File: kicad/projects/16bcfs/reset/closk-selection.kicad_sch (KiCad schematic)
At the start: 3 parts, among them U2 74HC00, U3 74HC08, U4 74HC32

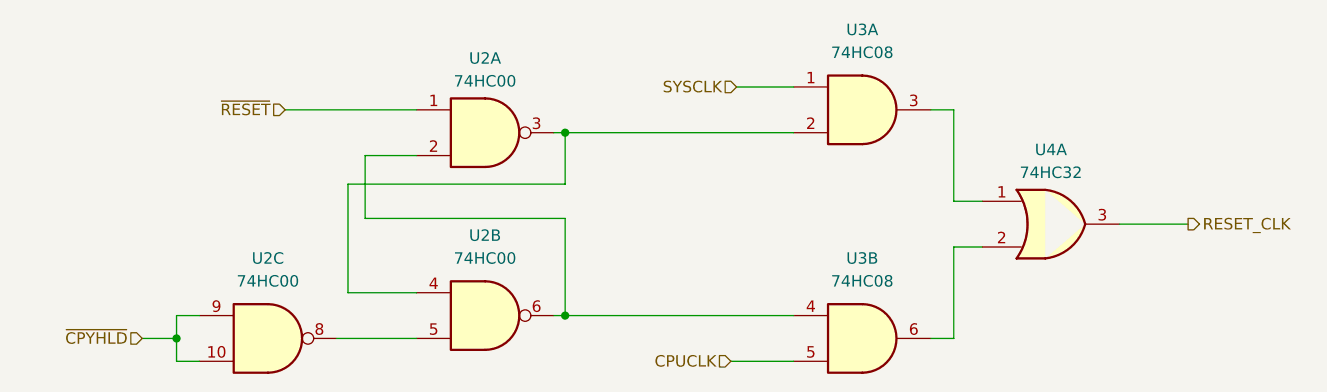
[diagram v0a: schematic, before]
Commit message: Added some debugging code
This is still not working.  I will need to revamp the reset routines for
the emulator to get this to work properly.  Everything will need an
initial state on construction and a `reset()` routine to place
everything into a proper state.  This in itself will be a major change.
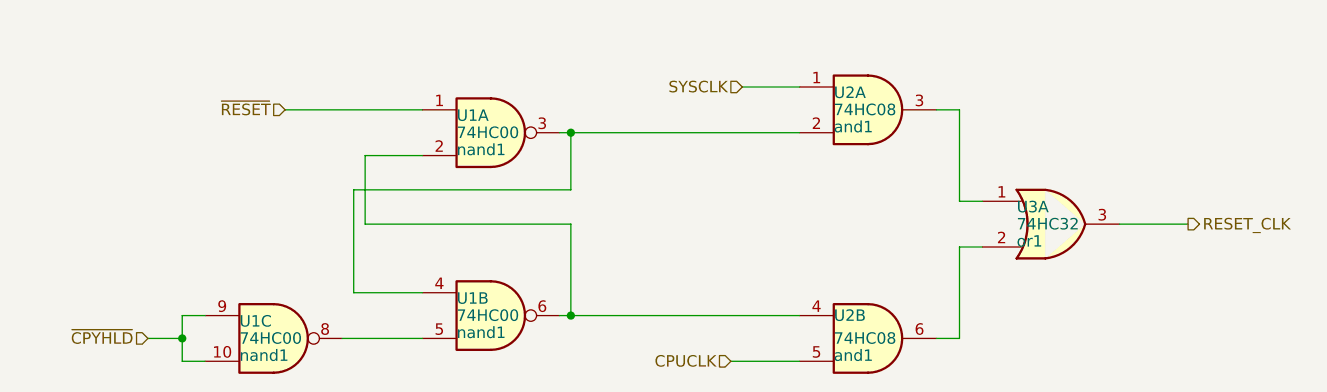
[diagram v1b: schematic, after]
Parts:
- U1: renamed from U2; name (none) -> nand1
- U2: renamed from U3; name (none) -> and1
- U3: renamed from U4; name (none) -> or1
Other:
- moved on the sheet: U1A, U1B, U1C, U2A, U2B

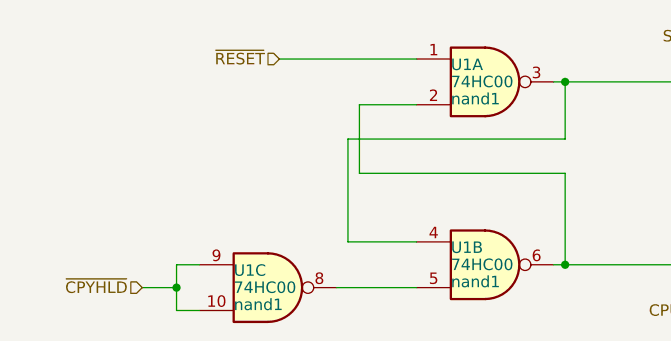
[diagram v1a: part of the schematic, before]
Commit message: Make a number of changes to the schematic and emulator
These changes are incremental to getting the emulator to work, they are
needed for making sure that the RESETTING, CLOCKING, and RUNNING signals
are processed properly.

There is also quite a bit of debugging code which gets added/removed
ahead of this commit.
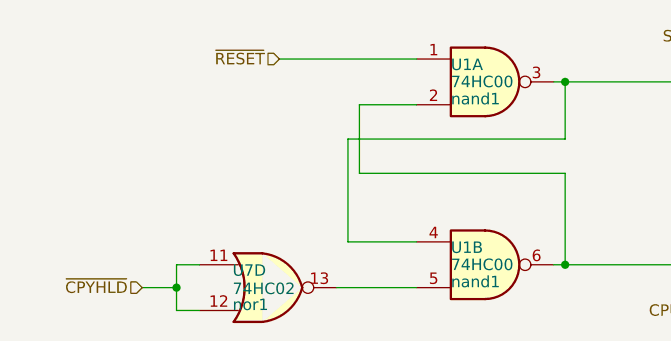
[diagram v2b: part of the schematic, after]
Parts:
- removed unit 3 of U1
- added U7: 74HC02, symbol 74xx:74HC02
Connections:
- net ~{CPYHLD}: now also U7.11, U7.12
- net at U1.5: now also U7.13

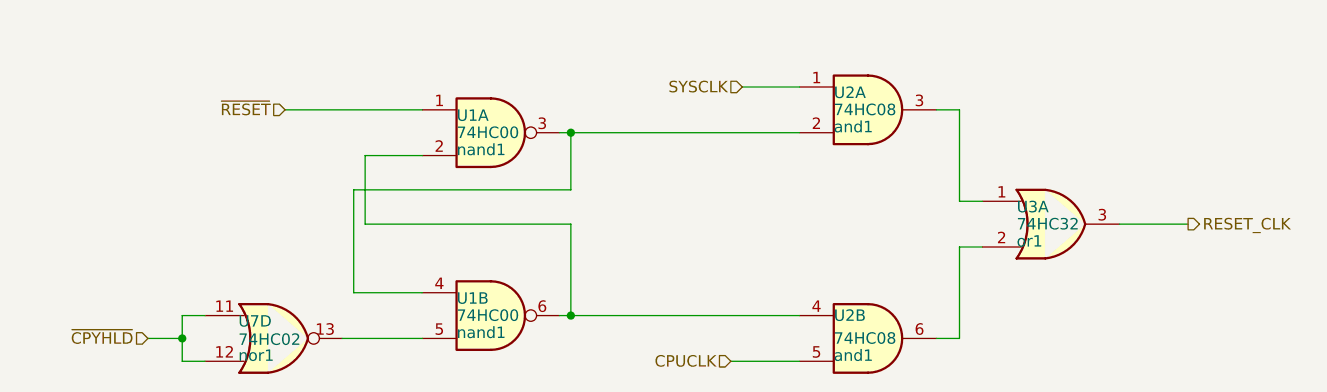
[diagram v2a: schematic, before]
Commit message: Relocate the unused gates for efficiency
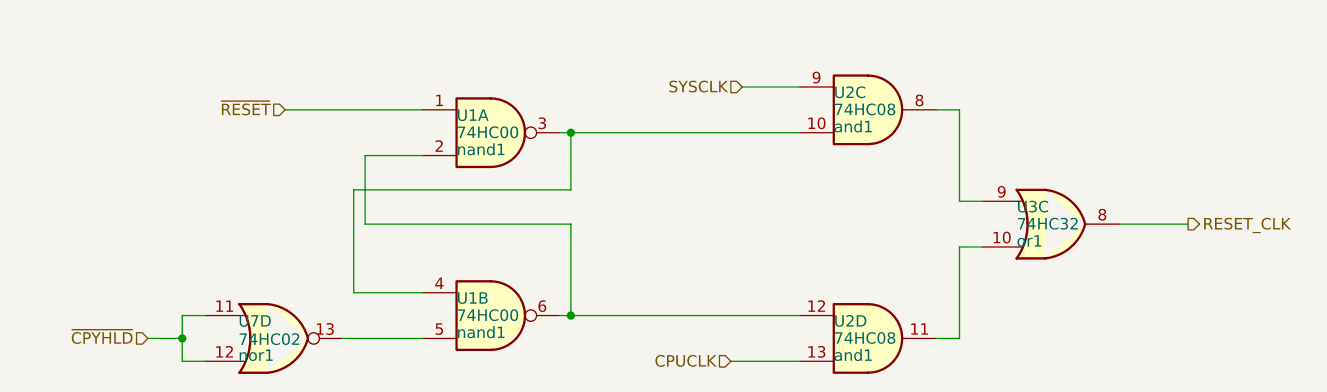
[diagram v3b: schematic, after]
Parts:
- removed U2: 74HC08, symbol eryjus:74HC08
- removed U3: 74HC32, symbol eryjus:74HC32
- added U2: 74HC08, symbol eryjus:74HC08
- added U3: 74HC32, symbol eryjus:74HC32
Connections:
- net CPUCLK: now also U2.13
- net RESET_CLK: now also U3.8
- net SYSCLK: now also U2.9
- net at U1.3, U1.4: now also U2.10
- net at U1.2, U1.6: now also U2.12
- new net: U2.8, U3.9
- new net: U2.11, U3.10
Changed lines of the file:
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@@
   (netclass_flag "" (length 2.54) (shape round) (at 190.5 90.17 180)
     (effects (font (size 1.27 1.27)) (justify right bottom))
-    (property "Netclass" "or1-Y1" (at 191.1985 92.71 0)
+    (property "Netclass" "or1-Y3" (at 191.1985 92.71 0)
       (effects (font (size 1.27 1.27) italic) (justify left))
     )
@@
   (netclass_flag "" (length 2.54) (shape round) (at 170.18 102.87 180)
     (effects (font (size 1.27 1.27)) (justify right bottom))
-    (property "Netclass" "and1-Y2" (at 170.8785 105.41 0)
+    (property "Netclass" "and1-Y3" (at 170.8785 105.41 0)
       (effects (font (size 1.27 1.27) italic) (justify left))
     )
@@
   (netclass_flag "" (length 2.54) (shape round) (at 170.18 77.47 0)
     (effects (font (size 1.27 1.27)) (justify left bottom))
-    (property "Netclass" "and1-Y1" (at 170.8785 74.93 0)
-      (effects (font (size 1.27 1.27) italic) (justify left))
+    (property "Netclass" "and1-Y3" (at 170.8785 74.93 0)
+      (effects (font (size 1.27 1.27) italic) (justify left))
+    )
+  )
+  (symbol (lib_id "eryjus:74HC08") (at 162.56 77.47 0) (unit 3)
+    (in_bom yes) (on_board yes) (dnp no)
+    (property "Reference" "U2" (at 158.75 75.565 0)
+      (effects (font (size 1.27 1.27)) (justify left))
+    )
+    (property "Value" "74HC08" (at 158.75 77.47 0)
+      (effects (font (size 1.27 1.27)) (justify left))
+    )
+    (property "Footprint" "" (at 162.56 77.47 0)
+      (effects (font (size 1.27 1.27)) hide)
+    )
+    (property "Datasheet" "http://www.ti.com/lit/gpn/sn74HC08" (at 162.56 77.47 0)
+      (effects (font (size 1.27 1.27)) hide)
+    )
+    (property "name" "and1" (at 158.75 79.375 0)
+      (effects (font (size 1.27 1.27)) (justify left))
+    )
+    (pin "13")
+    (pin "10")
+    (pin "1")
+    (pin "12")
+    (pin "6")
+    (pin "3")
+    (pin "7")
+    (pin "14")
+    (pin "4")
+    (pin "11")
+    (pin "2")
+    (pin "5")
+    (pin "9")
+    (pin "8")
+    (instances
+      (project "reset"
+        (path "/d0ae44e5-d74e-4df6-bf3d-e0535c5a7785/cb5fc007-d820-4dc1-be0b-c81376ce29c0"
+          (reference "U2") (unit 3)
+        )
+      )
+    )
+  )
+  (symbol (lib_id "eryjus:74HC32") (at 182.88 90.17 0) (unit 3)
+    (in_bom yes) (on_board yes) (dnp no)
+    (property "Reference" "U3" (at 179.07 88.265 0)
+      (effects (font (size 1.27 1.27)) (justify left))
+    )
+    (property "Value" "74HC32" (at 179.07 90.17 0)
+      (effects (font (size 1.27 1.27)) (justify left))
+    )
+    (property "Footprint" "" (at 182.88 90.17 0)
+      (effects (font (size 1.27 1.27)) hide)
+    )
+    (property "Datasheet" "http://www.ti.com/lit/gpn/sn74HC32" (at 182.88 90.17 0)
+      (effects (font (size 1.27 1.27)) hide)
+    )
+    (property "name" "or1" (at 179.07 92.075 0)
+      (effects (font (size 1.27 1.27)) (justify left))
+    )
+    (pin "5")
+    (pin "4")
+    (pin "12")
+    (pin "1")
+    (pin "11")
+    (pin "6")
+    (pin "3")
+    (pin "14")
+    (pin "13")
+    (pin "7")
+    (pin "10")
+    (pin "2")
+    (pin "8")
+    (pin "9")
+    (instances
+      (project "reset"
+        (path "/d0ae44e5-d74e-4df6-bf3d-e0535c5a7785/cb5fc007-d820-4dc1-be0b-c81376ce29c0"
+          (reference "U3") (unit 3)
+        )
+      )
     )
   )
@@
     )
   )
-  (symbol (lib_id "eryjus:74HC08") (at 162.56 77.47 0) (unit 1)
-    (in_bom yes) (on_board yes) (dnp no)
-    (property "Reference" "U2" (at 158.75 75.565 0)
-      (effects (font (size 1.27 1.27)) (justify left))
-    )
-    (property "Value" "74HC08" (at 158.75 77.47 0)
-      (effects (font (size 1.27 1.27)) (justify left))
-    )
-    (property "Footprint" "" (at 162.56 77.47 0)
-      (effects (font (size 1.27 1.27)) hide)
-    )
-    (property "Datasheet" "http://www.ti.com/lit/gpn/sn74HC08" (at 162.56 77.47 0)
-      (effects (font (size 1.27 1.27)) hide)
-    )
-    (property "name" "and1" (at 158.75 79.375 0)
-      (effects (font (size 1.27 1.27)) (justify left))
-    )
-    (pin "13")
-    (pin "10")
-    (pin "1")
-    (pin "12")
-    (pin "6")
-    (pin "3")
-    (pin "7")
-    (pin "14")
-    (pin "4")
-    (pin "11")
-    (pin "2")
-    (pin "5")
-    (pin "9")
-    (pin "8")
-    (instances
-      (project "reset"
-        (path "/d0ae44e5-d74e-4df6-bf3d-e0535c5a7785/cb5fc007-d820-4dc1-be0b-c81376ce29c0"
-          (reference "U2") (unit 1)
-        )
-      )
-    )
-  )
-  (symbol (lib_id "eryjus:74HC32") (at 182.88 90.17 0) (unit 1)
-    (in_bom yes) (on_board yes) (dnp no)
-    (property "Reference" "U3" (at 179.07 88.265 0)
-      (effects (font (size 1.27 1.27)) (justify left))
-    )
-    (property "Value" "74HC32" (at 179.07 90.17 0)
-      (effects (font (size 1.27 1.27)) (justify left))
-    )
-    (property "Footprint" "" (at 182.88 90.17 0)
-      (effects (font (size 1.27 1.27)) hide)
-    )
-    (property "Datasheet" "http://www.ti.com/lit/gpn/sn74HC32" (at 182.88 90.17 0)
-      (effects (font (size 1.27 1.27)) hide)
-    )
-    (property "name" "or1" (at 179.07 92.075 0)
-      (effects (font (size 1.27 1.27)) (justify left))
-    )
-    (pin "5")
-    (pin "4")
-    (pin "12")
-    (pin "1")
-    (pin "11")
-    (pin "6")
-    (pin "3")
-    (pin "14")
-    (pin "13")
-    (pin "7")
-    (pin "10")
-    (pin "2")
-    (pin "8")
-    (pin "9")
-    (instances
-      (project "reset"
-        (path "/d0ae44e5-d74e-4df6-bf3d-e0535c5a7785/cb5fc007-d820-4dc1-be0b-c81376ce29c0"
-          (reference "U3") (unit 1)
-        )
-      )
-    )
-  )
   (symbol (lib_id "74xx:74HC00") (at 120.65 80.01 0) (unit 1)
     (in_bom yes) (on_board yes) (dnp no)
@@
     )
   )
-  (symbol (lib_id "eryjus:74HC08") (at 162.56 102.87 0) (unit 2)
-    (in_bom yes) (on_board yes) (dnp no)
-    (property "Reference" "U2" (at 158.75 100.33 0)
+  (symbol (lib_id "eryjus:74HC08") (at 162.56 102.87 0) (unit 4)
+    (in_bom yes) (on_board yes) (dnp no)
+    (property "Reference" "U2" (at 158.75 100.965 0)
       (effects (font (size 1.27 1.27)) (justify left))
     )
@@
       (project "reset"
         (path "/d0ae44e5-d74e-4df6-bf3d-e0535c5a7785/cb5fc007-d820-4dc1-be0b-c81376ce29c0"
-          (reference "U2") (unit 2)
-        )
-      )
+          (reference "U2") (unit 4)
+        )
+      )

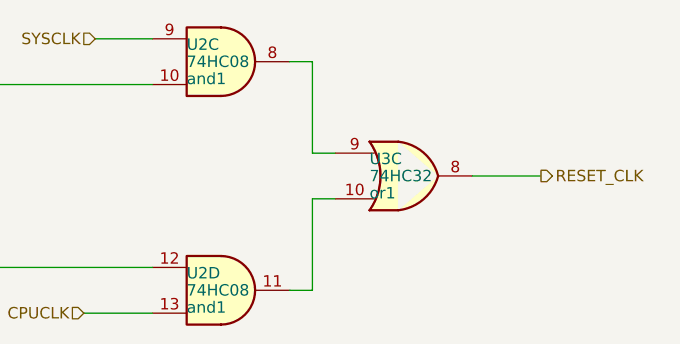
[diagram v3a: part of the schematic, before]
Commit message: Address some issues with the Reset Logic
There were a couple of fixes.  One in relation to how the 74xx123 IC was
emulated and others to the schematic to address issues in real life in
the breadboard prototype.
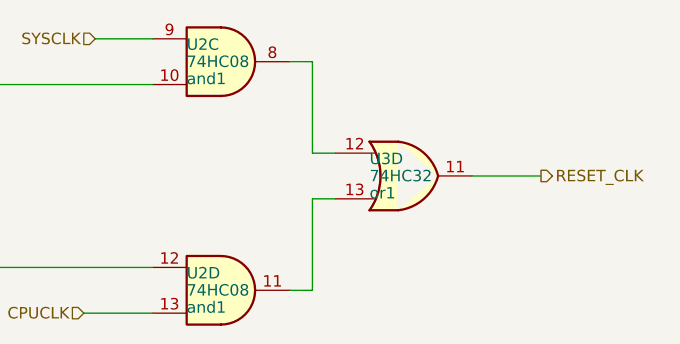
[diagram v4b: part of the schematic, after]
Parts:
- removed U3: 74HC32, symbol eryjus:74HC32
- added U3: 74HC32, symbol eryjus:74HC32
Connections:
- net RESET_CLK: now also U3.11
- net at U2.8: now also U3.12
- net at U2.11: now also U3.13
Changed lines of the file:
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@@
   (netclass_flag "" (length 2.54) (shape round) (at 190.5 90.17 180)
     (effects (font (size 1.27 1.27)) (justify right bottom))
-    (property "Netclass" "or1-Y3" (at 191.1985 92.71 0)
+    (property "Netclass" "or1-Y4" (at 191.1985 92.71 0)
       (effects (font (size 1.27 1.27) italic) (justify left))
     )
@@
     (property "Netclass" "and1-Y3" (at 170.8785 74.93 0)
       (effects (font (size 1.27 1.27) italic) (justify left))
+    )
+  )
+  (symbol (lib_id "eryjus:74HC32") (at 182.88 90.17 0) (unit 4)
+    (in_bom yes) (on_board yes) (dnp no)
+    (property "Reference" "U3" (at 179.07 88.265 0)
+      (effects (font (size 1.27 1.27)) (justify left))
+    )
+    (property "Value" "74HC32" (at 179.07 90.17 0)
+      (effects (font (size 1.27 1.27)) (justify left))
+    )
+    (property "Footprint" "" (at 182.88 90.17 0)
+      (effects (font (size 1.27 1.27)) hide)
+    )
+    (property "Datasheet" "http://www.ti.com/lit/gpn/sn74HC32" (at 182.88 90.17 0)
+      (effects (font (size 1.27 1.27)) hide)
+    )
+    (property "name" "or1" (at 179.07 92.075 0)
+      (effects (font (size 1.27 1.27)) (justify left))
+    )
+    (pin "5")
+    (pin "4")
+    (pin "12")
+    (pin "1")
+    (pin "11")
+    (pin "6")
+    (pin "3")
+    (pin "14")
+    (pin "13")
+    (pin "7")
+    (pin "10")
+    (pin "2")
+    (pin "8")
+    (pin "9")
+    (instances
+      (project "reset"
+        (path "/d0ae44e5-d74e-4df6-bf3d-e0535c5a7785/cb5fc007-d820-4dc1-be0b-c81376ce29c0"
+          (reference "U3") (unit 4)
+        )
+      )
     )
   )
@@
         )
       )
-    )
-  )
-  (symbol (lib_id "eryjus:74HC32") (at 182.88 90.17 0) (unit 3)
-    (in_bom yes) (on_board yes) (dnp no)
-    (property "Reference" "U3" (at 179.07 88.265 0)
-      (effects (font (size 1.27 1.27)) (justify left))
-    )
-    (property "Value" "74HC32" (at 179.07 90.17 0)
-      (effects (font (size 1.27 1.27)) (justify left))
-    )
-    (property "Footprint" "" (at 182.88 90.17 0)
-      (effects (font (size 1.27 1.27)) hide)
-    )
-    (property "Datasheet" "http://www.ti.com/lit/gpn/sn74HC32" (at 182.88 90.17 0)
-      (effects (font (size 1.27 1.27)) hide)
-    )
-    (property "name" "or1" (at 179.07 92.075 0)
-      (effects (font (size 1.27 1.27)) (justify left))
-    )
-    (pin "5")
-    (pin "4")
-    (pin "12")
-    (pin "1")
-    (pin "11")
-    (pin "6")
-    (pin "3")
-    (pin "14")
-    (pin "13")
-    (pin "7")
-    (pin "10")
-    (pin "2")
-    (pin "8")
-    (pin "9")
-    (instances
-      (project "reset"
-        (path "/d0ae44e5-d74e-4df6-bf3d-e0535c5a7785/cb5fc007-d820-4dc1-be0b-c81376ce29c0"
-          (reference "U3") (unit 3)
-        )
-      )

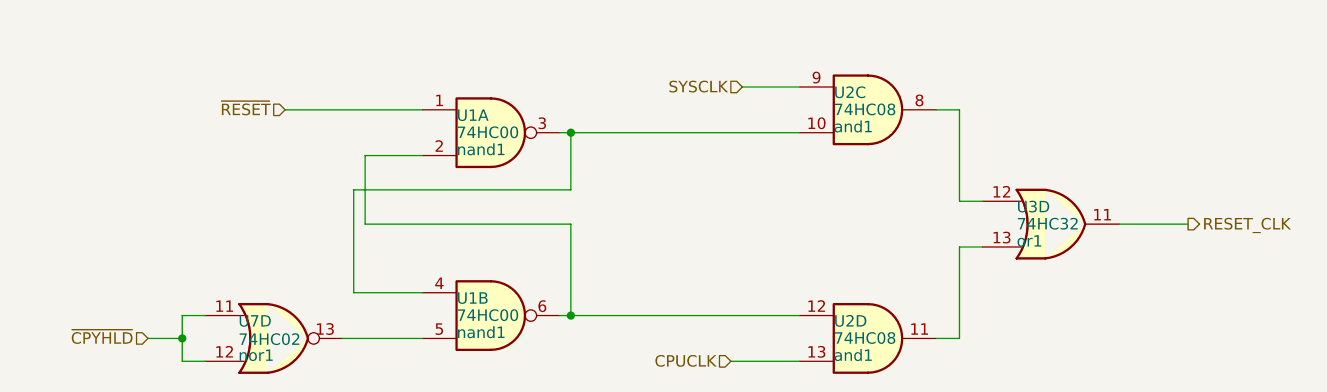
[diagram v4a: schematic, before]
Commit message: Rename RESET_CLK
This also forces a rename of the SYSCLK on the Reset Schematic to be
HS_CLK.  The new name of the RESET_CLK is SYS_CLK.
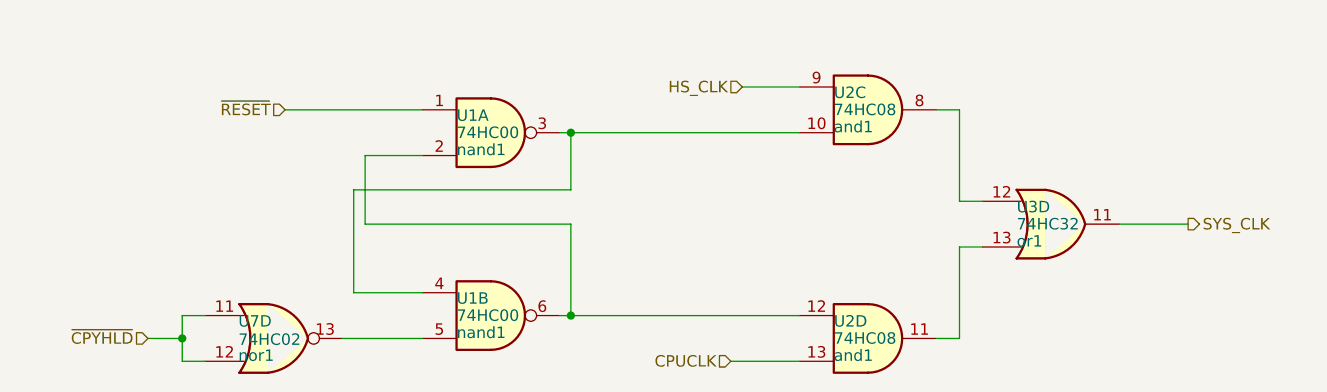
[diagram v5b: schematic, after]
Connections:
- net RESET_CLK renamed SYS_CLK
- net SYSCLK renamed HS_CLK
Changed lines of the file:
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@@
     (stroke (width 0) (type default))
   )
-  (hierarchical_label "SYSCLK" (shape input) (at 148.59 74.93 180) (fields_autoplaced)
+  (hierarchical_label "HS_CLK" (shape input) (at 148.59 74.93 180) (fields_autoplaced)
     (effects (font (size 1.27 1.27)) (justify right))
   )
-  (hierarchical_label "RESET_CLK" (shape output) (at 198.12 90.17 0) (fields_autoplaced)
+  (hierarchical_label "SYS_CLK" (shape output) (at 198.12 90.17 0) (fields_autoplaced)
     (effects (font (size 1.27 1.27)) (justify left))
   )

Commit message: Some KiCad Cleanup
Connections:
- net SYS_CLK renamed CLK
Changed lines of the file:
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@@
     (effects (font (size 1.27 1.27)) (justify right))
   )
-  (hierarchical_label "SYS_CLK" (shape output) (at 198.12 90.17 0) (fields_autoplaced)
+  (hierarchical_label "CLK" (shape output) (at 198.12 90.17 0) (fields_autoplaced)
     (effects (font (size 1.27 1.27)) (justify left))
   )
